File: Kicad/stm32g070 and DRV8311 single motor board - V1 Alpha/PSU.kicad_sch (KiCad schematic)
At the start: 31 parts, among them Q1 NMOS, SQS142ENW, Q2 NMOS, Q3 PMOS,SiSS61DN, Q4 PMOS, U3 BQ298012RUGT, U4 BQ25060

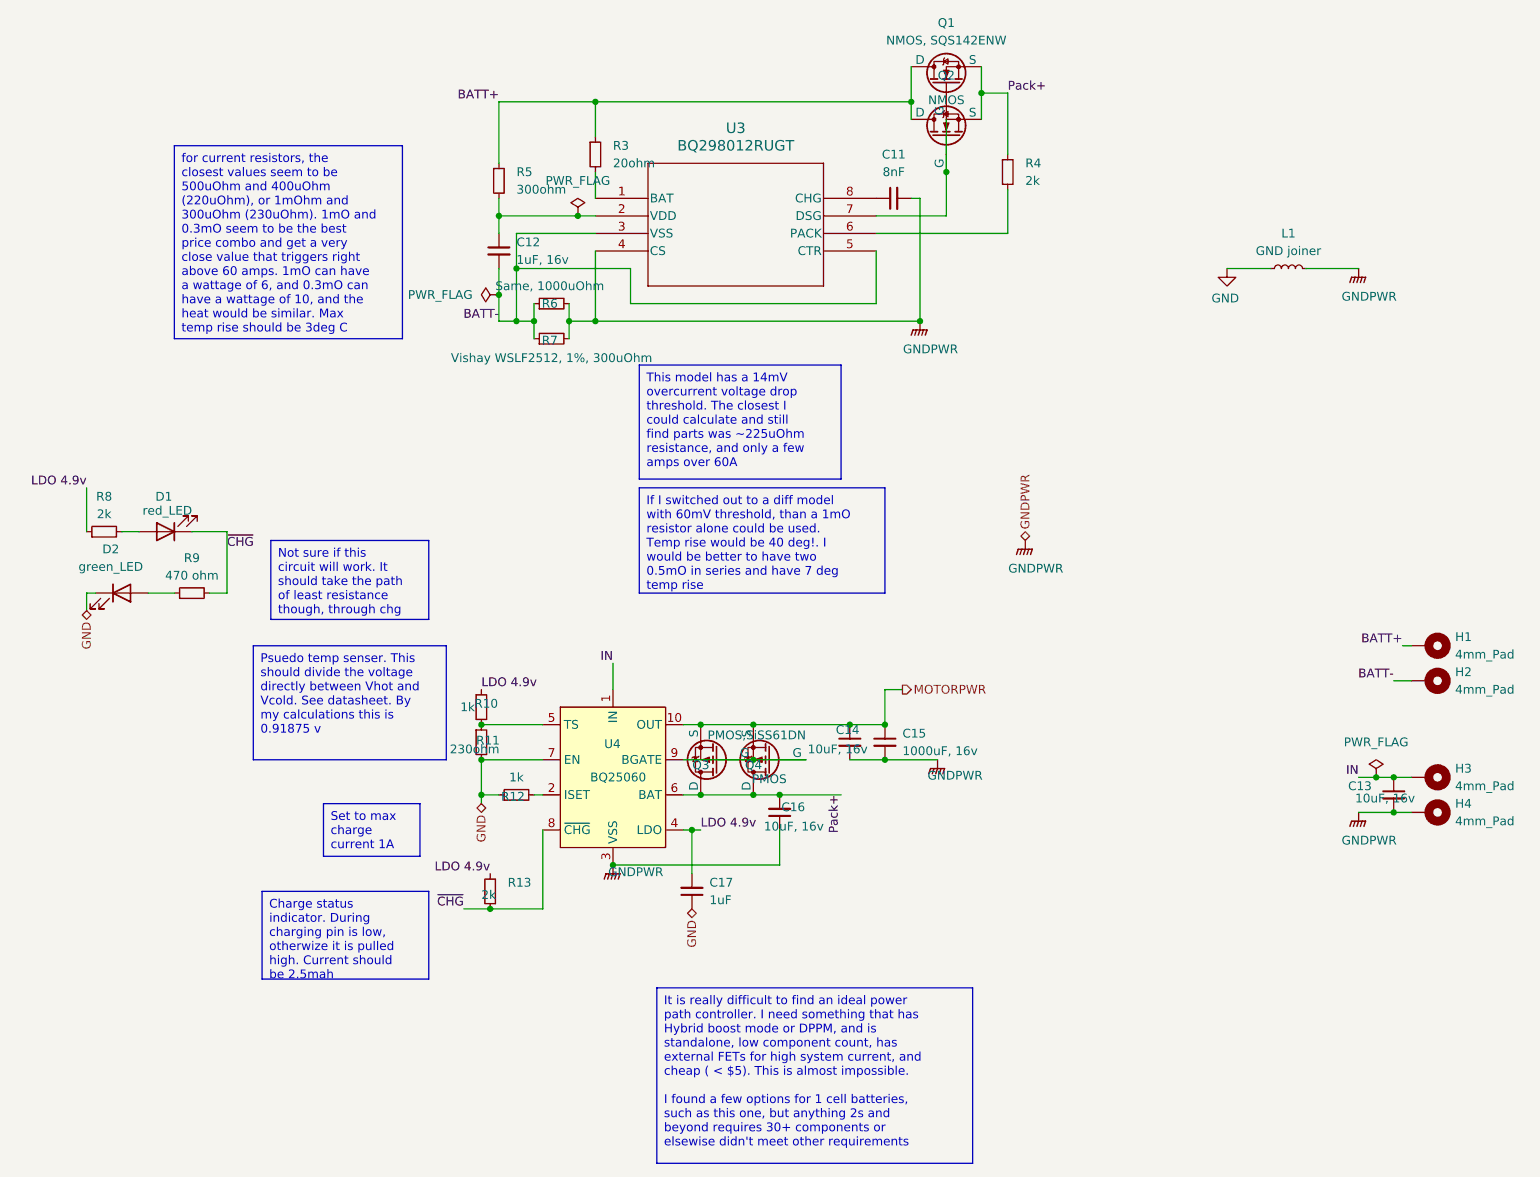
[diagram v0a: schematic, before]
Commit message: Fixes to the PCB after production related to mosfets
So..... I sourced the wrong mosfets. I chose mosfets with the marketing moniker PowerPAK, never thinking that could mean multiple footprint sizes. I sourced mosfets with the powerpak 1212 footprint, instead of the powerpak SO-8 footprint. They ended up being tiny and I had to do a bodge fix to test. I have replaced the mosfets in schematic with correctly sized ones now.

Another change I made in this commit is related to LEDs. I sourced the leds and resistors last minute, so the values are a bit different than originally on the schematic. I realized too that my tri-state led status circuit wouldn't work, because the bq25060 status pin is not a tri-state and I couldn't make it one. I now only have one led to indicate charging. I have updated the schematics and board with the values and single status led.

The big capacitors I sourced differently, I wasn't able to get a small 220uF, so I got a big aluminum polarized 220uF and put it in place of the 1000uF. All the other capacitors are different too, I realized the voltage rating doesn't matter on some, so to cut down BOM part number if there was a capacitor value with two separate voltages, I just went with 16v one.

Gerber files have been updated.
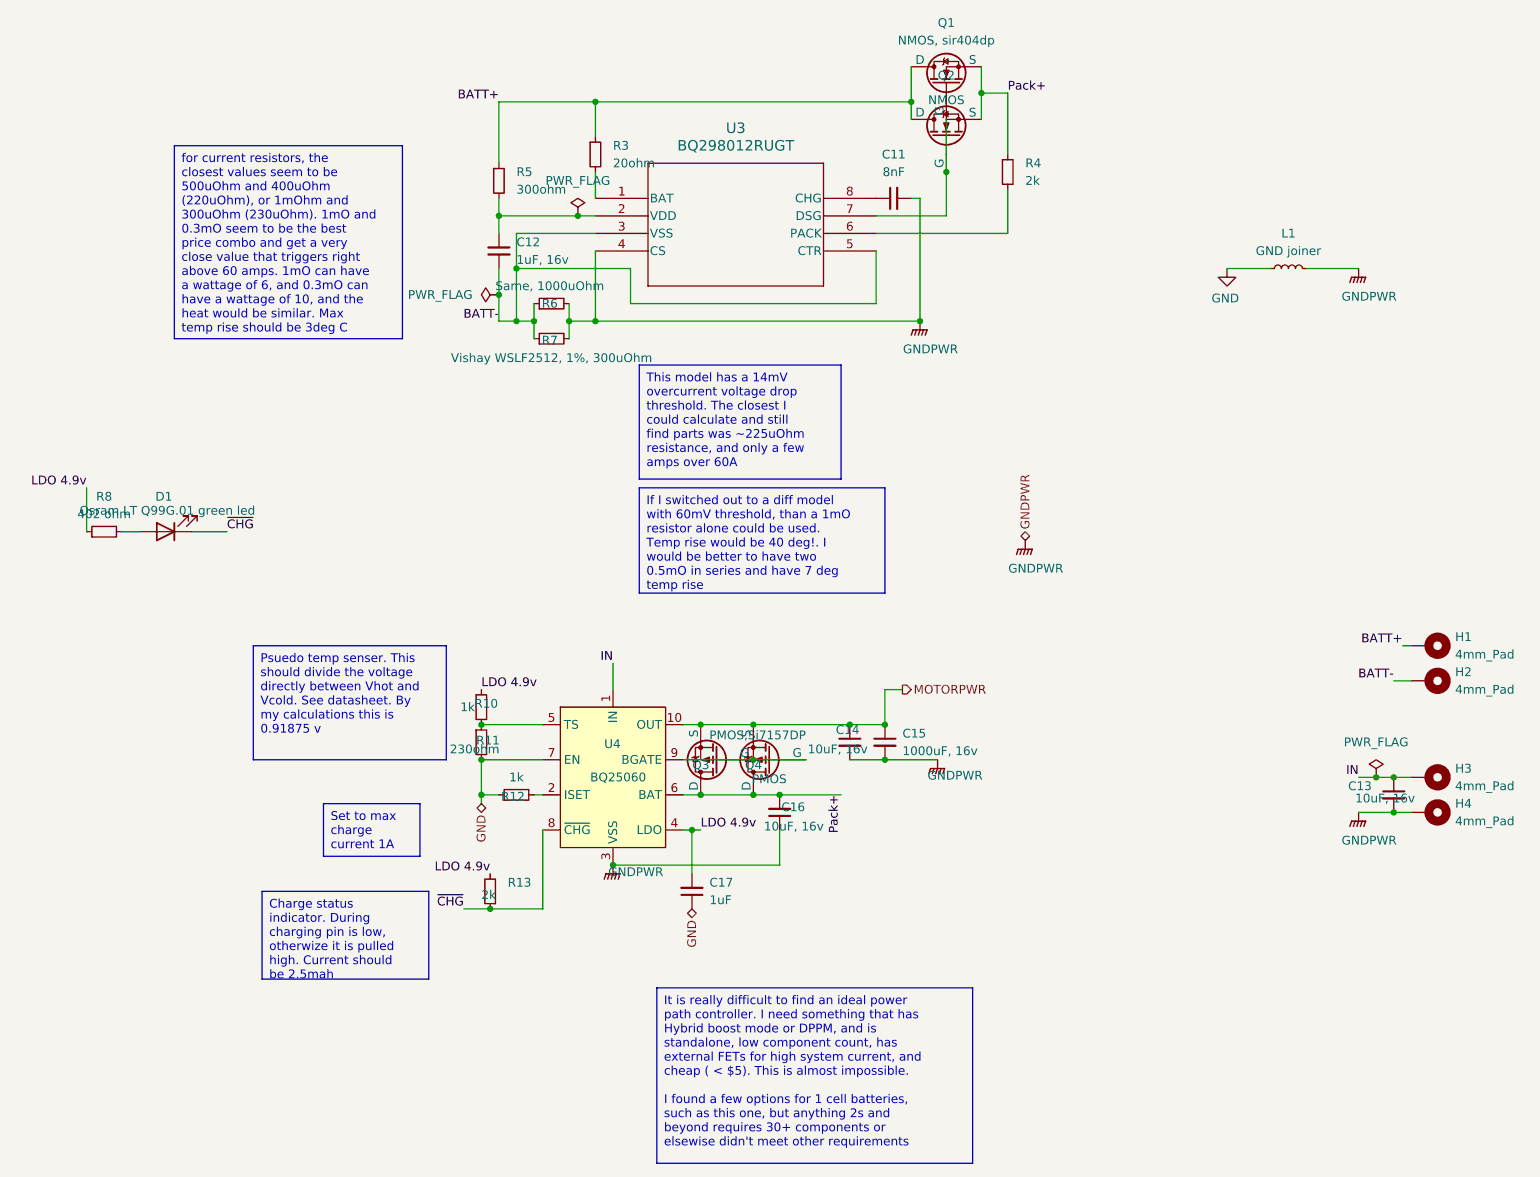
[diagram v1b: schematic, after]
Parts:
- removed D2: green_LED, LED_SMD:LED_0603_1608Metric_Pad1.05x0.95mm_HandSolder, symbol Device:LED
- removed R9: 470 ohm, Resistor_SMD:R_0603_1608Metric, symbol Device:R_Small
- D1: value red_LED -> Osram LT Q99G.01 green led
- Q1: value NMOS, SQS142ENW -> NMOS, sir404dp
- Q3: value PMOS,SiSS61DN -> PMOS,Si7157DP
- R8: value 2k -> 402 ohm
